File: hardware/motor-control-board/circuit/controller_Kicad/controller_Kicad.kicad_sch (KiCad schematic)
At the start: 26 parts, among them CN1 2510-4AW, CN2 2510-4AW, SW1 SS-12D10L5, U1 XIAO_RP2040_SEEED, U2 POLOLU_A4988_DRIVER, U3 POLOLU_A4988_DRIVER

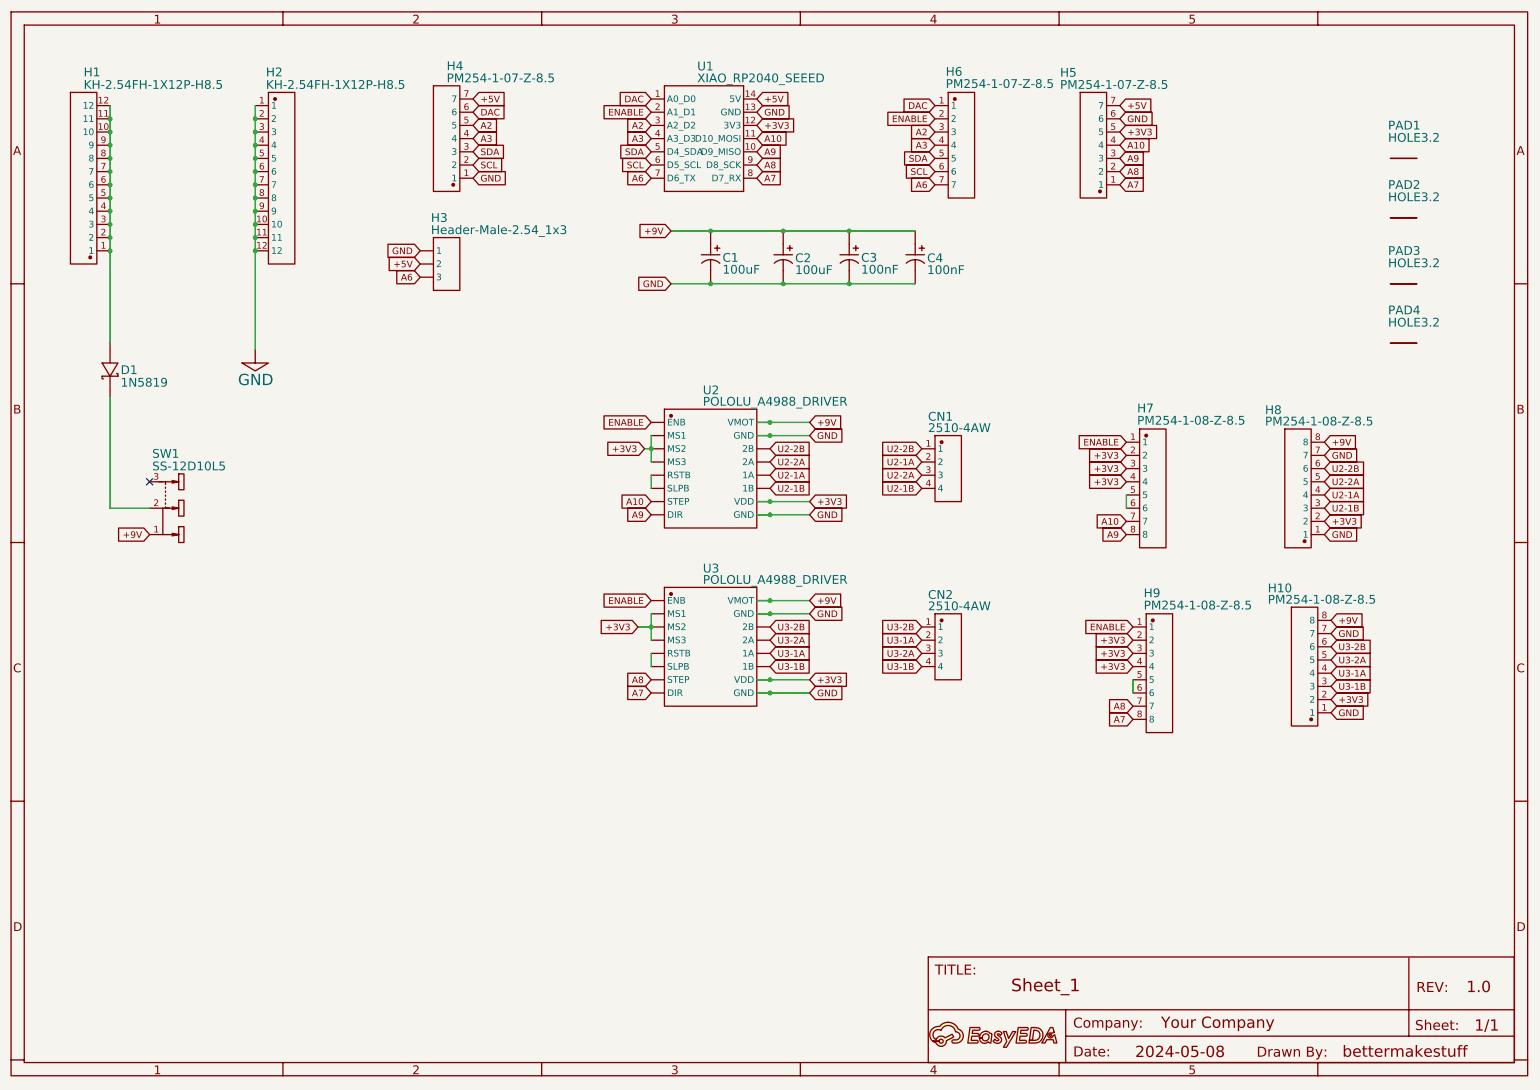
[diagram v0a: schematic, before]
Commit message: re-laid out and re-routed PCB - V1.0 ready for production
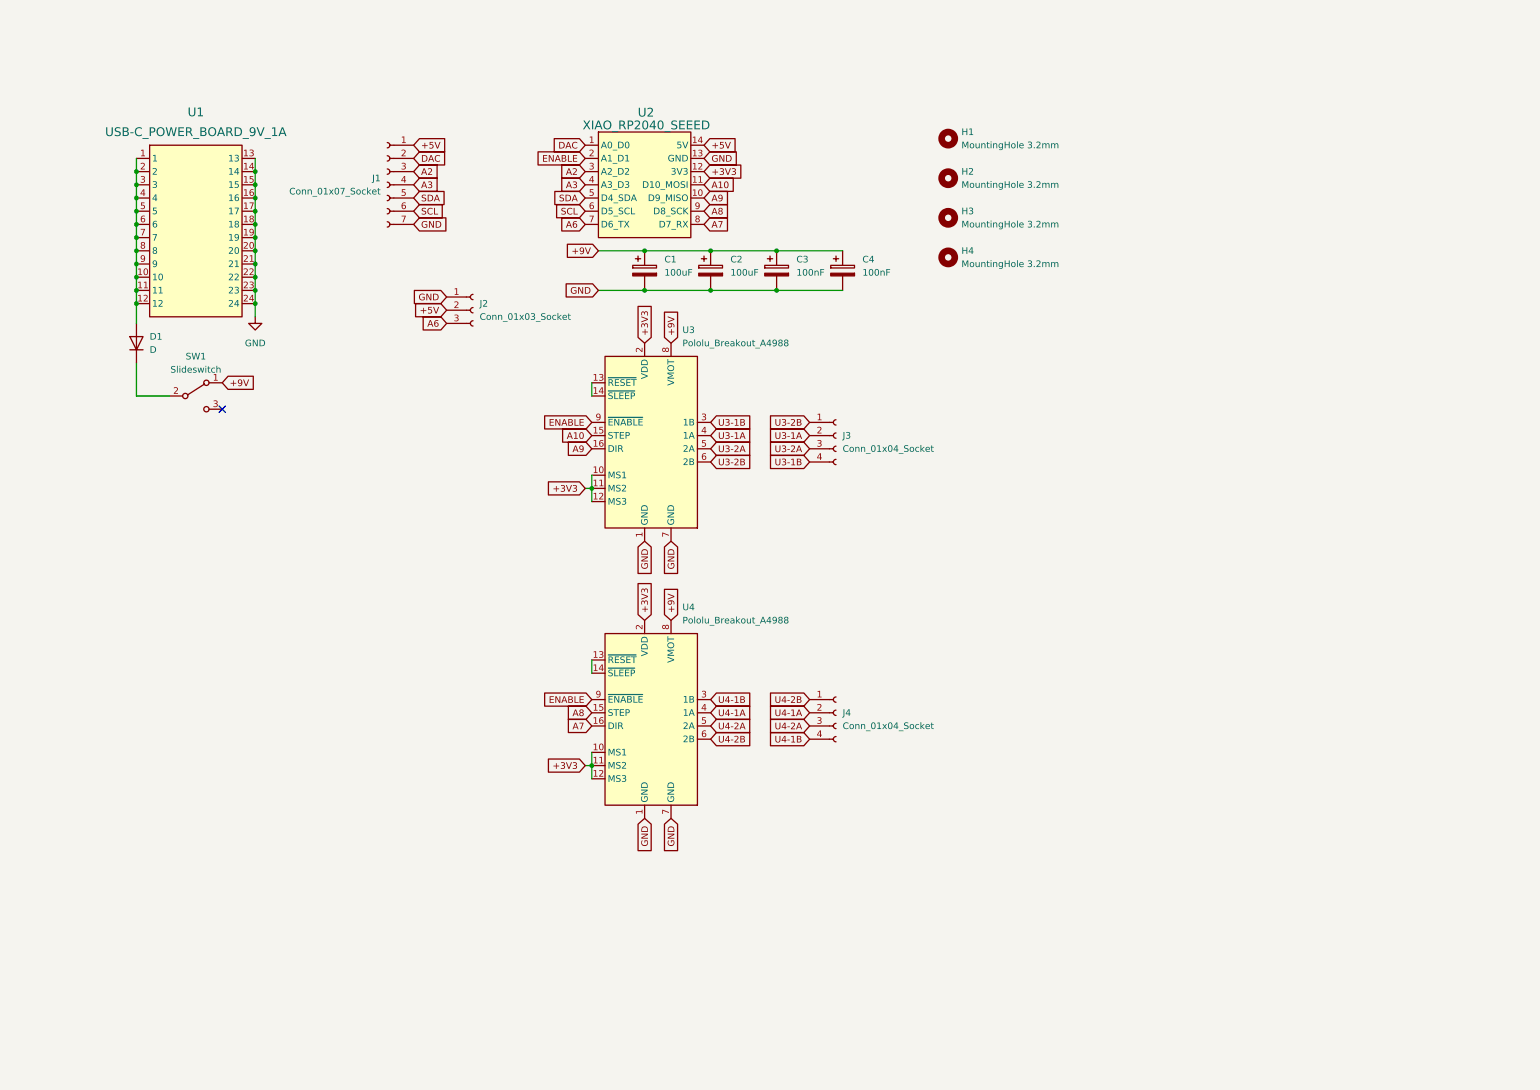
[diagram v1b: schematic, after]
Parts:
- removed A1: A, symbol Unknown_0_-806
- removed C1: 100uF, Library:CP_Radial_D8.0mm_P2.50mm_Horizontal_Mirrored, symbol CA45-A-35V-0.1UF-K
- removed C2: 100uF, Library:CP_Radial_D8.0mm_P2.50mm_Horizontal_Mirrored, symbol RST100UF25V004
- removed C3: 100nF, Capacitor_THT:C_Disc_D4.3mm_W1.9mm_P5.00mm, symbol CA45-A-35V-0.1UF-K_1
- removed C4: 100nF, Capacitor_THT:C_Disc_D4.3mm_W1.9mm_P5.00mm, symbol RST100UF25V004_1
- removed CN1: 2510-4AW, Connector_PinHeader_2.54mm:PinHeader_1x04_P2.54mm_Horizontal, symbol 2510-4AW
- removed CN2: 2510-4AW, Connector_PinHeader_2.54mm:PinHeader_1x04_P2.54mm_Horizontal, symbol 2510-4AW_1
- removed D1: 1N5819, Diode_THT:D_DO-35_SOD27_P7.62mm_Horizontal, symbol SS510_C466506
- removed H1: KH-2.54FH-1X12P-H8.5, Connector_PinSocket_2.54mm:PinSocket_1x12_P2.54mm_Vertical, symbol KH-2.54FH-1X12P-H8.5
- removed H10: PM254-1-08-Z-8.5, Connector_PinSocket_2.54mm:PinSocket_1x08_P2.54mm_Vertical, symbol PM254-1-08-Z-8.5_3
- removed H2: KH-2.54FH-1X12P-H8.5, Connector_PinSocket_2.54mm:PinSocket_1x12_P2.54mm_Vertical, symbol KH-2.54FH-1X12P-H8.5_1
- removed H3: Header-Male-2.54_1x3, symbol Header-Male-2.54_1x3
- removed H4: PM254-1-07-Z-8.5, symbol PM254-1-07-Z-8.5
- removed H5: PM254-1-07-Z-8.5, Connector_PinSocket_2.54mm:PinSocket_1x07_P2.54mm_Vertical, symbol PM254-1-07-Z-8.5_1
- removed H6: PM254-1-07-Z-8.5, Connector_PinSocket_2.54mm:PinSocket_1x07_P2.54mm_Vertical, symbol PM254-1-07-Z-8.5_2
- removed H7: PM254-1-08-Z-8.5, Connector_PinSocket_2.54mm:PinSocket_1x08_P2.54mm_Vertical, symbol PM254-1-08-Z-8.5
- removed H8: PM254-1-08-Z-8.5, Connector_PinSocket_2.54mm:PinSocket_1x08_P2.54mm_Vertical, symbol PM254-1-08-Z-8.5_1
- removed H9: PM254-1-08-Z-8.5, Connector_PinSocket_2.54mm:PinSocket_1x08_P2.54mm_Vertical, symbol PM254-1-08-Z-8.5_2
- removed PAD1: HOLE3.2, Library:HOLE-3.2MM, symbol HOLE3.2
- removed PAD2: HOLE3.2, Library:HOLE-3.2MM, symbol HOLE3.2_1
- removed PAD3: HOLE3.2, Library:HOLE-3.2MM, symbol HOLE3.2_2
- removed PAD4: HOLE3.2, Library:HOLE-3.2MM, symbol HOLE3.2_3
- removed SW1: SS-12D10L5, Library:SW_Slide-03_Wuerth-WS-SLTV_10x2.5x6.4_P2.54mm_Pins_1_2_Reversed, symbol SS-12D10L5
- removed U1: XIAO_RP2040_SEEED, symbol XIAO_RP2040_SEEED
- removed U2: POLOLU_A4988_DRIVER, symbol POLOLU_A4988_DRIVER
- removed U3: POLOLU_A4988_DRIVER, symbol POLOLU_A4988_DRIVER_1
- added C1, C2: 100uF, Library:CP_Radial_D8.0mm_P2.50mm_Horizontal_Mirrored, symbol Device:C_Polarized
- added C3, C4: 100nF, Capacitor_THT:C_Disc_D4.3mm_W1.9mm_P5.00mm, symbol Device:C_Polarized
- added D1: D, Diode_THT:D_DO-35_SOD27_P7.62mm_Horizontal, symbol Device:D
- added H1, H2, H3, H4: MountingHole 3.2mm, Library:HOLE-3.2MM, symbol Mechanical:MountingHole
- added J1: Conn_01x07_Socket, Connector_PinSocket_2.54mm:PinSocket_1x07_P2.54mm_Vertical, symbol Connector:Conn_01x07_Socket
- added J2: Conn_01x03_Socket, Connector_PinSocket_2.54mm:PinSocket_1x03_P2.54mm_Vertical, symbol Connector:Conn_01x03_Socket
- added J3, J4: Conn_01x04_Socket, Connector_PinHeader_2.54mm:PinHeader_1x04_P2.54mm_Horizontal, symbol Connector:Conn_01x04_Socket
- added SW1: Slideswitch, Library:SW_Slide-03_Wuerth-WS-SLTV_10x2.5x6.4_P2.54mm_Pins_1_2_Reversed, symbol fab:SWITCH_AYZ0102AGRLC
- added U1: USB-C_POWER_BOARD_9V_1A, Library:USB-C_POWER_BOARD_9V_1A, symbol Library:USB-C_POWER_BOARD_9V_1A
- added U2: XIAO_RP2040_SEEED, Library:XIAO_RP2040_SEEED, symbol XIAO_RP2040_SEEED
- added U3, U4: Pololu_Breakout_A4988, Module:Pololu_Breakout-16_15.2x20.3mm, symbol Driver_Motor:Pololu_Breakout_A4988
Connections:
- net +3V3: now also U2.12 (3V3), U3.10 (MS1), U3.11 (MS2), U3.12 (MS3), U3.2 (VDD), U4.10 (MS1), U4.11 (MS2), U4.12 (MS3), U4.2 (VDD)
- net +5V: now also J1.1 (Pin_1), J2.2 (Pin_2), U2.14 (5V)
- net +9V: now also C1.1, C2.1, C3.1, C4.1, SW1.1 (A), U3.8 (VMOT), U4.8 (VMOT)
- net A10: now also U2.11 (D10_MOSI), U3.15 (STEP)
- net A2: now also J1.3 (Pin_3), U2.3 (A2_D2)
- net A3: now also J1.4 (Pin_4), U2.4 (A3_D3)
- net A6: now also J2.3 (Pin_3), U2.7 (D6_TX)
- net A7: now also U2.8 (D7_RX), U4.16 (DIR)
- net A8: now also U2.9 (D8_SCK), U4.15 (STEP)
- net A9: now also U2.10 (D9_MISO), U3.16 (DIR)
- net DAC: now also J1.2 (Pin_2), U2.1 (A0_D0)
- net ENABLE: now also U2.2 (A1_D1), U3.9 (~{ENABLE}), U4.9 (~{ENABLE})
- net GND: now also C1.2, C2.2, C3.2, C4.2, J1.7 (Pin_7), J2.1 (Pin_1), U1.13, U1.14, U1.15, U1.16, U1.17, U1.18, U1.19, U1.20, U1.21, U1.22, U1.23, U1.24, U2.13 (GND), U3.1 (GND), U3.7 (GND), U4.1 (GND), U4.7 (GND)
- net SCL: now also J1.6 (Pin_6), U2.6 (D5_SCL)
- net SDA: now also J1.5 (Pin_5), U2.5 (D4_SDA)
- net U3-1A: now also J3.2 (Pin_2), U3.4 (1A)
- net U3-1B: now also J3.4 (Pin_4), U3.3 (1B)
- net U3-2A: now also J3.3 (Pin_3), U3.5 (2A)
- net U3-2B: now also J3.1 (Pin_1), U3.6 (2B)
- new net: U4.13 (~{RESET}), U4.14 (~{SLEEP})
- new net: U3.13 (~{RESET}), U3.14 (~{SLEEP})
- new net: D1.1 (K), SW1.2 (B)
- new net: D1.2 (A), U1.1, U1.10, U1.11, U1.12, U1.2, U1.3, U1.4, U1.5, U1.6, U1.7, U1.8, U1.9
- new net U4-1A: J4.2 (Pin_2), U4.4 (1A)
- new net U4-1B: J4.4 (Pin_4), U4.3 (1B)
- new net U4-2A: J4.3 (Pin_3), U4.5 (2A)
- new net U4-2B: J4.1 (Pin_1), U4.6 (2B)
